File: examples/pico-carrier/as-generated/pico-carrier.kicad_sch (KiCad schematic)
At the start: 13 parts, among them J1 5V IN, J3 GP0-GP15, J4 GP16-GP28, PWR, U1 Pico

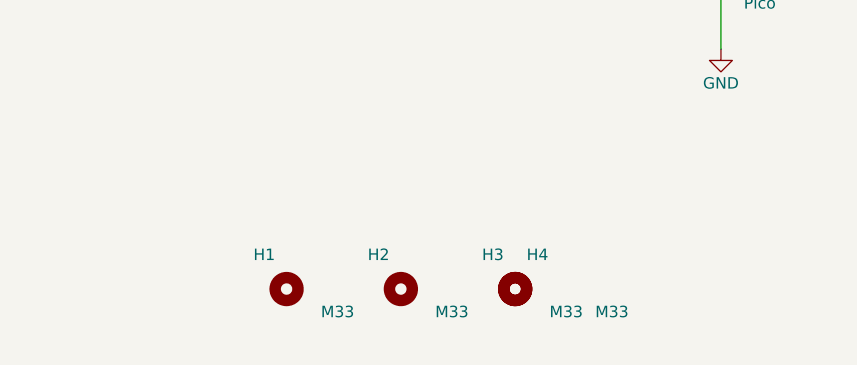
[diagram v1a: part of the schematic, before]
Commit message: Give the assembly machine something to aim at
Fiducials: three copper dots in bare mask windows, near three different
corners so a pick-and-place gets rotation as well as offset. It aligns
to the board, not to the drawing - without them it has only the routed
outline, cut to a tolerance ten times looser than the placement a 0.5 mm
pitch part is asking for. `fab.no_fiducials` reports a fine-pitch board
that has none, as context rather than as a fault: plenty of boards are
built one at a time with tweezers.

They share the corner search with the mounting holes, which is where
this found a real bug: `_courtyard_box` read lines and rectangles only,
and a mounting hole draws its courtyard as one circle - so every hole
measured as taking up no room at all, and the first three fiducials
landed on top of three screw holes. Circles and arcs count now.

Co-Authored-By: Claude Fable 5 <noreply@anthropic.com>
Claude-Session: https://claude.ai/code/session_01DUj7Ltu92tWg159mCSacwY
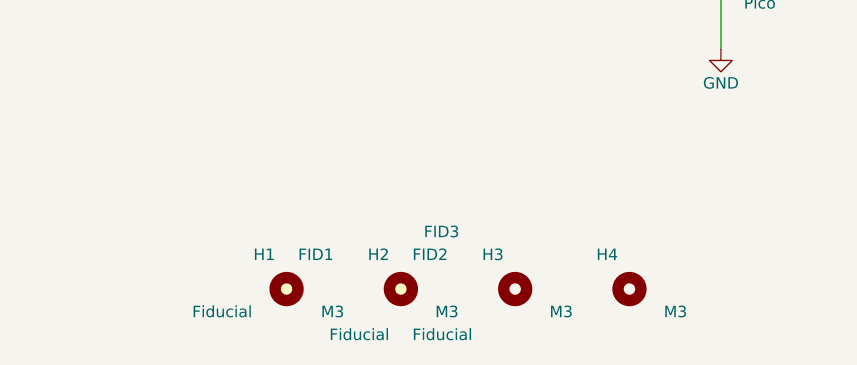
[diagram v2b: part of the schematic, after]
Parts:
- added FID1, FID2, FID3: Fiducial, Fiducial:Fiducial_1mm_Mask2mm, symbol Mechanical:Fiducial
- H1, H2, H3, H4: value M33 -> M3
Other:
- moved on the sheet: H4
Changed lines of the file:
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@@
     (exclude_from_sim no) (in_bom yes) (on_board yes) (dnp no)
     (property "Reference" "H1" (at 100.64 166.18 0) (effects (font (size 1.27 1.27)) (justify right)))
-    (property "Value" "M33" (at 105.72 172.53 0) (effects (font (size 1.27 1.27)) (justify left)))
+    (property "Value" "M3" (at 105.72 172.53 0) (effects (font (size 1.27 1.27)) (justify left)))
     (property "Footprint" "MountingHole:MountingHole_3.2mm_M3" (at 101.91 169.99 0) (effects (font (size 1.27 1.27)) hide))
     (property "Datasheet" "~" (at 101.91 169.99 0) (effects (font (size 1.27 1.27)) hide))
@@
     (exclude_from_sim no) (in_bom yes) (on_board yes) (dnp no)
     (property "Reference" "H2" (at 113.34 166.18 0) (effects (font (size 1.27 1.27)) (justify right)))
-    (property "Value" "M33" (at 118.42 172.53 0) (effects (font (size 1.27 1.27)) (justify left)))
+    (property "Value" "M3" (at 118.42 172.53 0) (effects (font (size 1.27 1.27)) (justify left)))
     (property "Footprint" "MountingHole:MountingHole_3.2mm_M3" (at 114.61 169.99 0) (effects (font (size 1.27 1.27)) hide))
     (property "Datasheet" "~" (at 114.61 169.99 0) (effects (font (size 1.27 1.27)) hide))
@@
     (exclude_from_sim no) (in_bom yes) (on_board yes) (dnp no)
     (property "Reference" "H3" (at 126.04 166.18 0) (effects (font (size 1.27 1.27)) (justify right)))
-    (property "Value" "M33" (at 131.12 172.53 0) (effects (font (size 1.27 1.27)) (justify left)))
+    (property "Value" "M3" (at 131.12 172.53 0) (effects (font (size 1.27 1.27)) (justify left)))
     (property "Footprint" "MountingHole:MountingHole_3.2mm_M3" (at 127.31 169.99 0) (effects (font (size 1.27 1.27)) hide))
     (property "Datasheet" "~" (at 127.31 169.99 0) (effects (font (size 1.27 1.27)) hide))
     (instances (project "pico-carrier" (path "/f86b03a2-2f64-5dc5-a6a7-b575bc25ae3a" (reference "H3") (unit 1))))
   )
-  (symbol (lib_id "Mechanical:MountingHole") (at 127.31 169.99 0.0) (unit 1)
+  (symbol (lib_id "Mechanical:MountingHole") (at 140.01 169.99 0.0) (unit 1)
     (exclude_from_sim no) (in_bom yes) (on_board yes) (dnp no)
-    (property "Reference" "H4" (at 128.58 166.18 0) (effects (font (size 1.27 1.27)) (justify left)))
-    (property "Value" "M33" (at 136.2 172.53 0) (effects (font (size 1.27 1.27)) (justify left)))
-    (property "Footprint" "MountingHole:MountingHole_3.2mm_M3" (at 127.31 169.99 0) (effects (font (size 1.27 1.27)) hide))
-    (property "Datasheet" "~" (at 127.31 169.99 0) (effects (font (size 1.27 1.27)) hide))
+    (property "Reference" "H4" (at 138.74 166.18 0) (effects (font (size 1.27 1.27)) (justify right)))
+    (property "Value" "M3" (at 143.82 172.53 0) (effects (font (size 1.27 1.27)) (justify left)))
+    (property "Footprint" "MountingHole:MountingHole_3.2mm_M3" (at 140.01 169.99 0) (effects (font (size 1.27 1.27)) hide))
+    (property "Datasheet" "~" (at 140.01 169.99 0) (effects (font (size 1.27 1.27)) hide))
     (instances (project "pico-carrier" (path "/f86b03a2-2f64-5dc5-a6a7-b575bc25ae3a" (reference "H4") (unit 1))))
   )
+  (symbol (lib_id "Mechanical:Fiducial") (at 101.91 169.99 0.0) (unit 1)
+    (exclude_from_sim no) (in_bom yes) (on_board yes) (dnp no)
+    (property "Reference" "FID1" (at 103.18 166.18 0) (effects (font (size 1.27 1.27)) (justify left)))
+    (property "Value" "Fiducial" (at 98.1 172.53 0) (effects (font (size 1.27 1.27)) (justify right)))
+    (property "Footprint" "Fiducial:Fiducial_1mm_Mask2mm" (at 101.91 169.99 0) (effects (font (size 1.27 1.27)) hide))
+    (property "Datasheet" "~" (at 101.91 169.99 0) (effects (font (size 1.27 1.27)) hide))
+    (instances (project "pico-carrier" (path "/f86b03a2-2f64-5dc5-a6a7-b575bc25ae3a" (reference "FID1") (unit 1))))
+  )
+  (symbol (lib_id "Mechanical:Fiducial") (at 114.61 169.99 0.0) (unit 1)
+    (exclude_from_sim no) (in_bom yes) (on_board yes) (dnp no)
+    (property "Reference" "FID2" (at 115.88 166.18 0) (effects (font (size 1.27 1.27)) (justify left)))
+    (property "Value" "Fiducial" (at 115.88 175.07 0) (effects (font (size 1.27 1.27)) (justify left)))
+    (property "Footprint" "Fiducial:Fiducial_1mm_Mask2mm" (at 114.61 169.99 0) (effects (font (size 1.27 1.27)) hide))
+    (property "Datasheet" "~" (at 114.61 169.99 0) (effects (font (size 1.27 1.27)) hide))
+    (instances (project "pico-carrier" (path "/f86b03a2-2f64-5dc5-a6a7-b575bc25ae3a" (reference "FID2") (unit 1))))
+  )
+  (symbol (lib_id "Mechanical:Fiducial") (at 114.61 169.99 0.0) (unit 1)
+    (exclude_from_sim no) (in_bom yes) (on_board yes) (dnp no)
+    (property "Reference" "FID3" (at 117.15 163.64 0) (effects (font (size 1.27 1.27)) (justify left)))
+    (property "Value" "Fiducial" (at 113.34 175.07 0) (effects (font (size 1.27 1.27)) (justify right)))
+    (property "Footprint" "Fiducial:Fiducial_1mm_Mask2mm" (at 114.61 169.99 0) (effects (font (size 1.27 1.27)) hide))
+    (property "Datasheet" "~" (at 114.61 169.99 0) (effects (font (size 1.27 1.27)) hide))
+    (instances (project "pico-carrier" (path "/f86b03a2-2f64-5dc5-a6a7-b575bc25ae3a" (reference "FID3") (unit 1))))
+  )
   (wire (pts (xy 72.7 82.36) (xy 80.32 82.36)) (stroke (width 0) (type default)))

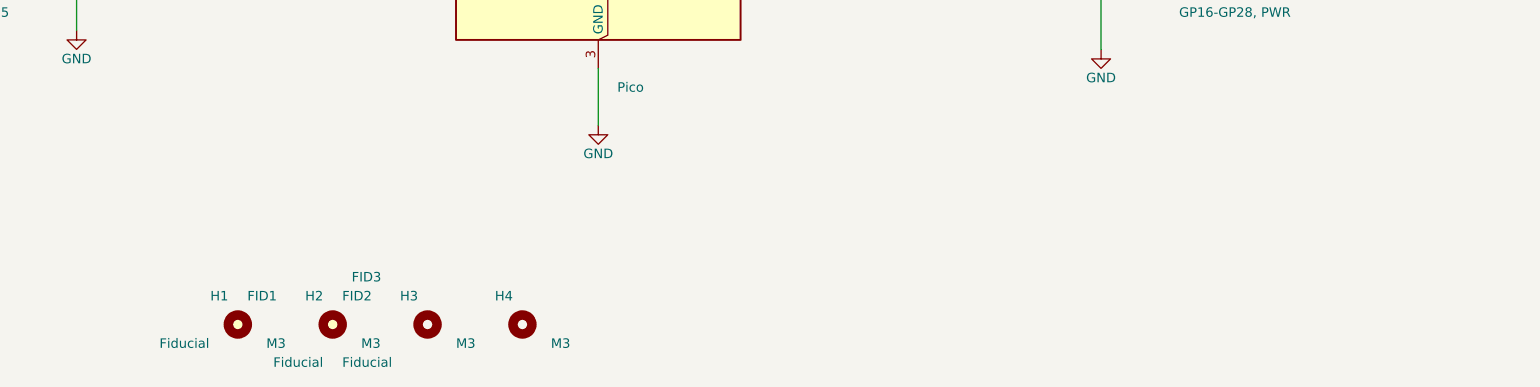
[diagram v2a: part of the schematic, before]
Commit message: Let the new parts sit somewhere sensible, on the board and on the sheet
Placing screw holes and fiducials turned up four things that were wrong
before either existed, all of them about where something is allowed to
go rather than about the parts themselves.

A designator was kept off the pads but not inside the board outline, so
any part at the edge - a connector, and now a hole - had its reference
clipped by the edge. Every board had been carrying one or two of those.

A symbol with no pins leaves no trace in the sheet planner's obstacle
list, because that list is built from pin stubs. The screw holes were
invisible to it and the fiducials landed on top of them. The free-row
search also ran off the right-hand edge of an A4 page and sat over the
title block on the way, which is `readability.outside_page` and
`readability.margin_intrusion` respectively - both real, both now
avoided by bounding the search to the drawing area.

And the bill-of-materials flag is read from the footprint rather than
the symbol library, because the footprint is the side KiCad's parity
check reads and the side the fab agrees with. That retired three
warnings the op-amp board had been carrying since it gained test
points: `Connector:TestPoint` claims to be a BOM line and its own
footprint says otherwise.

All four fast boards pass their gates; the suite is green on 10.0.4.

Co-Authored-By: Claude Fable 5 <noreply@anthropic.com>
Claude-Session: https://claude.ai/code/session_01DUj7Ltu92tWg159mCSacwY
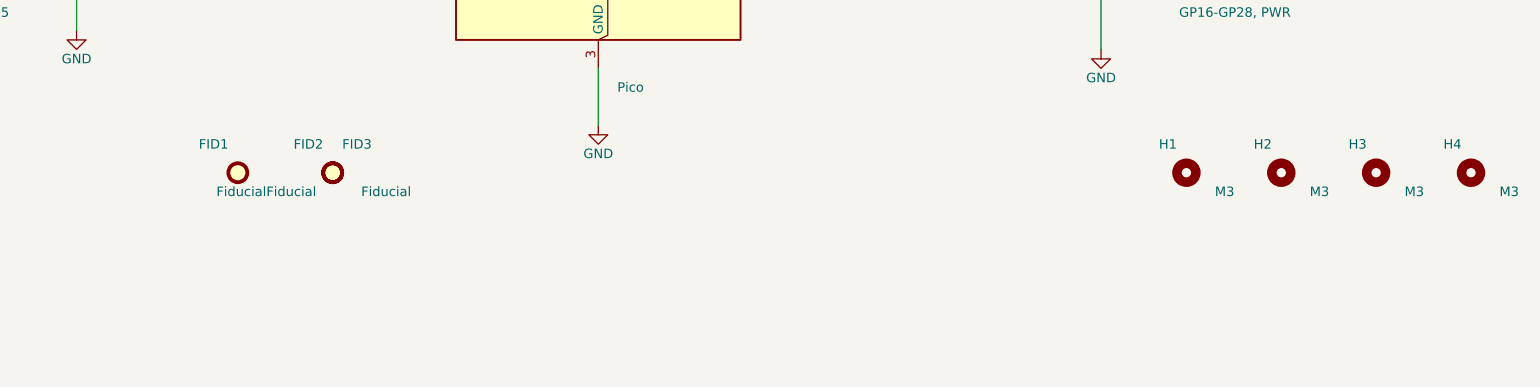
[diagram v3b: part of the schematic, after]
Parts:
- FID1, FID2, FID3, H1, H2, H3, H4: now left out of the parts list
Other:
- moved on the sheet: FID1, FID2, FID3, H1, H2, H3, H4
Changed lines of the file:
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@@
     (instances (project "pico-carrier" (path "/f86b03a2-2f64-5dc5-a6a7-b575bc25ae3a" (reference "D3") (unit 1))))
   )
-  (symbol (lib_id "Mechanical:MountingHole") (at 101.91 169.99 0.0) (unit 1)
-    (exclude_from_sim no) (in_bom yes) (on_board yes) (dnp no)
-    (property "Reference" "H1" (at 100.64 166.18 0) (effects (font (size 1.27 1.27)) (justify right)))
-    (property "Value" "M3" (at 105.72 172.53 0) (effects (font (size 1.27 1.27)) (justify left)))
-    (property "Footprint" "MountingHole:MountingHole_3.2mm_M3" (at 101.91 169.99 0) (effects (font (size 1.27 1.27)) hide))
-    (property "Datasheet" "~" (at 101.91 169.99 0) (effects (font (size 1.27 1.27)) hide))
+  (symbol (lib_id "Mechanical:MountingHole") (at 228.91 149.67 0.0) (unit 1)
+    (exclude_from_sim no) (in_bom no) (on_board yes) (dnp no)
+    (property "Reference" "H1" (at 227.64 145.86 0) (effects (font (size 1.27 1.27)) (justify right)))
+    (property "Value" "M3" (at 232.72 152.21 0) (effects (font (size 1.27 1.27)) (justify left)))
+    (property "Footprint" "MountingHole:MountingHole_3.2mm_M3" (at 228.91 149.67 0) (effects (font (size 1.27 1.27)) hide))
+    (property "Datasheet" "~" (at 228.91 149.67 0) (effects (font (size 1.27 1.27)) hide))
     (instances (project "pico-carrier" (path "/f86b03a2-2f64-5dc5-a6a7-b575bc25ae3a" (reference "H1") (unit 1))))
   )
-  (symbol (lib_id "Mechanical:MountingHole") (at 114.61 169.99 0.0) (unit 1)
-    (exclude_from_sim no) (in_bom yes) (on_board yes) (dnp no)
-    (property "Reference" "H2" (at 113.34 166.18 0) (effects (font (size 1.27 1.27)) (justify right)))
-    (property "Value" "M3" (at 118.42 172.53 0) (effects (font (size 1.27 1.27)) (justify left)))
-    (property "Footprint" "MountingHole:MountingHole_3.2mm_M3" (at 114.61 169.99 0) (effects (font (size 1.27 1.27)) hide))
-    (property "Datasheet" "~" (at 114.61 169.99 0) (effects (font (size 1.27 1.27)) hide))
+  (symbol (lib_id "Mechanical:MountingHole") (at 241.61 149.67 0.0) (unit 1)
+    (exclude_from_sim no) (in_bom no) (on_board yes) (dnp no)
+    (property "Reference" "H2" (at 240.34 145.86 0) (effects (font (size 1.27 1.27)) (justify right)))
+    (property "Value" "M3" (at 245.42 152.21 0) (effects (font (size 1.27 1.27)) (justify left)))
+    (property "Footprint" "MountingHole:MountingHole_3.2mm_M3" (at 241.61 149.67 0) (effects (font (size 1.27 1.27)) hide))
+    (property "Datasheet" "~" (at 241.61 149.67 0) (effects (font (size 1.27 1.27)) hide))
     (instances (project "pico-carrier" (path "/f86b03a2-2f64-5dc5-a6a7-b575bc25ae3a" (reference "H2") (unit 1))))
   )
-  (symbol (lib_id "Mechanical:MountingHole") (at 127.31 169.99 0.0) (unit 1)
-    (exclude_from_sim no) (in_bom yes) (on_board yes) (dnp no)
-    (property "Reference" "H3" (at 126.04 166.18 0) (effects (font (size 1.27 1.27)) (justify right)))
-    (property "Value" "M3" (at 131.12 172.53 0) (effects (font (size 1.27 1.27)) (justify left)))
-    (property "Footprint" "MountingHole:MountingHole_3.2mm_M3" (at 127.31 169.99 0) (effects (font (size 1.27 1.27)) hide))
-    (property "Datasheet" "~" (at 127.31 169.99 0) (effects (font (size 1.27 1.27)) hide))
+  (symbol (lib_id "Mechanical:MountingHole") (at 254.31 149.67 0.0) (unit 1)
+    (exclude_from_sim no) (in_bom no) (on_board yes) (dnp no)
+    (property "Reference" "H3" (at 253.04 145.86 0) (effects (font (size 1.27 1.27)) (justify right)))
+    (property "Value" "M3" (at 258.12 152.21 0) (effects (font (size 1.27 1.27)) (justify left)))
+    (property "Footprint" "MountingHole:MountingHole_3.2mm_M3" (at 254.31 149.67 0) (effects (font (size 1.27 1.27)) hide))
+    (property "Datasheet" "~" (at 254.31 149.67 0) (effects (font (size 1.27 1.27)) hide))
     (instances (project "pico-carrier" (path "/f86b03a2-2f64-5dc5-a6a7-b575bc25ae3a" (reference "H3") (unit 1))))
   )
-  (symbol (lib_id "Mechanical:MountingHole") (at 140.01 169.99 0.0) (unit 1)
-    (exclude_from_sim no) (in_bom yes) (on_board yes) (dnp no)
-    (property "Reference" "H4" (at 138.74 166.18 0) (effects (font (size 1.27 1.27)) (justify right)))
-    (property "Value" "M3" (at 143.82 172.53 0) (effects (font (size 1.27 1.27)) (justify left)))
-    (property "Footprint" "MountingHole:MountingHole_3.2mm_M3" (at 140.01 169.99 0) (effects (font (size 1.27 1.27)) hide))
-    (property "Datasheet" "~" (at 140.01 169.99 0) (effects (font (size 1.27 1.27)) hide))
+  (symbol (lib_id "Mechanical:MountingHole") (at 267.01 149.67 0.0) (unit 1)
+    (exclude_from_sim no) (in_bom no) (on_board yes) (dnp no)
+    (property "Reference" "H4" (at 265.74 145.86 0) (effects (font (size 1.27 1.27)) (justify right)))
+    (property "Value" "M3" (at 270.82 152.21 0) (effects (font (size 1.27 1.27)) (justify left)))
+    (property "Footprint" "MountingHole:MountingHole_3.2mm_M3" (at 267.01 149.67 0) (effects (font (size 1.27 1.27)) hide))
+    (property "Datasheet" "~" (at 267.01 149.67 0) (effects (font (size 1.27 1.27)) hide))
     (instances (project "pico-carrier" (path "/f86b03a2-2f64-5dc5-a6a7-b575bc25ae3a" (reference "H4") (unit 1))))
   )
-  (symbol (lib_id "Mechanical:Fiducial") (at 101.91 169.99 0.0) (unit 1)
-    (exclude_from_sim no) (in_bom yes) (on_board yes) (dnp no)
-    (property "Reference" "FID1" (at 103.18 166.18 0) (effects (font (size 1.27 1.27)) (justify left)))
-    (property "Value" "Fiducial" (at 98.1 172.53 0) (effects (font (size 1.27 1.27)) (justify right)))
-    (property "Footprint" "Fiducial:Fiducial_1mm_Mask2mm" (at 101.91 169.99 0) (effects (font (size 1.27 1.27)) hide))
-    (property "Datasheet" "~" (at 101.91 169.99 0) (effects (font (size 1.27 1.27)) hide))
+  (symbol (lib_id "Mechanical:Fiducial") (at 101.91 149.67 0.0) (unit 1)
+    (exclude_from_sim no) (in_bom no) (on_board yes) (dnp no)
+    (property "Reference" "FID1" (at 100.64 145.86 0) (effects (font (size 1.27 1.27)) (justify right)))
+    (property "Value" "Fiducial" (at 105.72 152.21 0) (effects (font (size 1.27 1.27)) (justify left)))
+    (property "Footprint" "Fiducial:Fiducial_1mm_Mask2mm" (at 101.91 149.67 0) (effects (font (size 1.27 1.27)) hide))
+    (property "Datasheet" "~" (at 101.91 149.67 0) (effects (font (size 1.27 1.27)) hide))
     (instances (project "pico-carrier" (path "/f86b03a2-2f64-5dc5-a6a7-b575bc25ae3a" (reference "FID1") (unit 1))))
   )
-  (symbol (lib_id "Mechanical:Fiducial") (at 114.61 169.99 0.0) (unit 1)
-    (exclude_from_sim no) (in_bom yes) (on_board yes) (dnp no)
-    (property "Reference" "FID2" (at 115.88 166.18 0) (effects (font (size 1.27 1.27)) (justify left)))
-    (property "Value" "Fiducial" (at 115.88 175.07 0) (effects (font (size 1.27 1.27)) (justify left)))
-    (property "Footprint" "Fiducial:Fiducial_1mm_Mask2mm" (at 114.61 169.99 0) (effects (font (size 1.27 1.27)) hide))
-    (property "Datasheet" "~" (at 114.61 169.99 0) (effects (font (size 1.27 1.27)) hide))
+  (symbol (lib_id "Mechanical:Fiducial") (at 114.61 149.67 0.0) (unit 1)
+    (exclude_from_sim no) (in_bom no) (on_board yes) (dnp no)
+    (property "Reference" "FID2" (at 113.34 145.86 0) (effects (font (size 1.27 1.27)) (justify right)))
+    (property "Value" "Fiducial" (at 118.42 152.21 0) (effects (font (size 1.27 1.27)) (justify left)))
+    (property "Footprint" "Fiducial:Fiducial_1mm_Mask2mm" (at 114.61 149.67 0) (effects (font (size 1.27 1.27)) hide))
+    (property "Datasheet" "~" (at 114.61 149.67 0) (effects (font (size 1.27 1.27)) hide))
     (instances (project "pico-carrier" (path "/f86b03a2-2f64-5dc5-a6a7-b575bc25ae3a" (reference "FID2") (unit 1))))
   )
-  (symbol (lib_id "Mechanical:Fiducial") (at 114.61 169.99 0.0) (unit 1)
-    (exclude_from_sim no) (in_bom yes) (on_board yes) (dnp no)
-    (property "Reference" "FID3" (at 117.15 163.64 0) (effects (font (size 1.27 1.27)) (justify left)))
-    (property "Value" "Fiducial" (at 113.34 175.07 0) (effects (font (size 1.27 1.27)) (justify right)))
-    (property "Footprint" "Fiducial:Fiducial_1mm_Mask2mm" (at 114.61 169.99 0) (effects (font (size 1.27 1.27)) hide))
-    (property "Datasheet" "~" (at 114.61 169.99 0) (effects (font (size 1.27 1.27)) hide))
+  (symbol (lib_id "Mechanical:Fiducial") (at 114.61 149.67 0.0) (unit 1)
+    (exclude_from_sim no) (in_bom no) (on_board yes) (dnp no)
+    (property "Reference" "FID3" (at 115.88 145.86 0) (effects (font (size 1.27 1.27)) (justify left)))
+    (property "Value" "Fiducial" (at 105.72 152.21 0) (effects (font (size 1.27 1.27)) (justify right)))
+    (property "Footprint" "Fiducial:Fiducial_1mm_Mask2mm" (at 114.61 149.67 0) (effects (font (size 1.27 1.27)) hide))
+    (property "Datasheet" "~" (at 114.61 149.67 0) (effects (font (size 1.27 1.27)) hide))
     (instances (project "pico-carrier" (path "/f86b03a2-2f64-5dc5-a6a7-b575bc25ae3a" (reference "FID3") (unit 1))))
   )
